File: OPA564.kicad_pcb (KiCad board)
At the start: 2 copper layers, 111 x 61 mm, 29 parts, among them J1 Conn_Coaxial, J4 Conn_Coaxial, J6 Conn_Coaxial, U1 OPA564AIDWPR, U2 OPA564AIDWPR, U3 OPA564AIDWPR

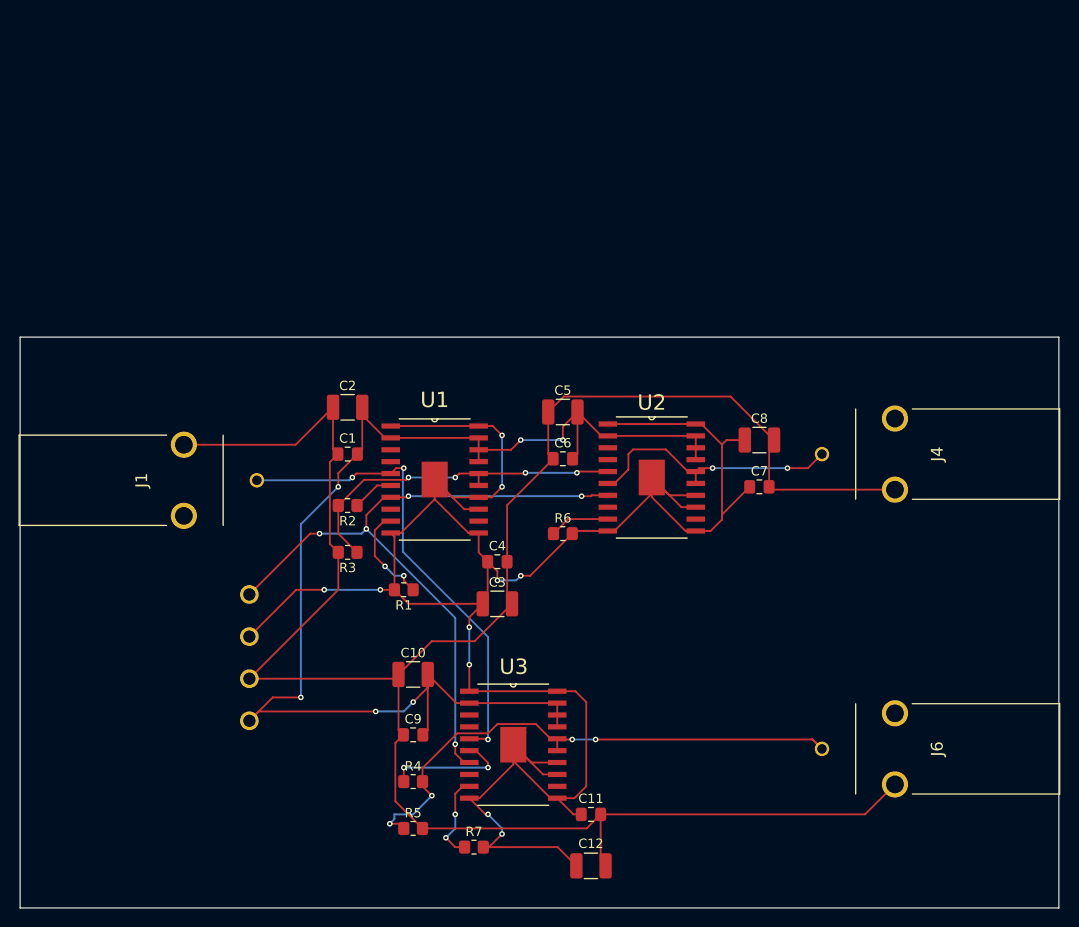
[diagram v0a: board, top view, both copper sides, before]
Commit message: OPA564 without Voltage Follower
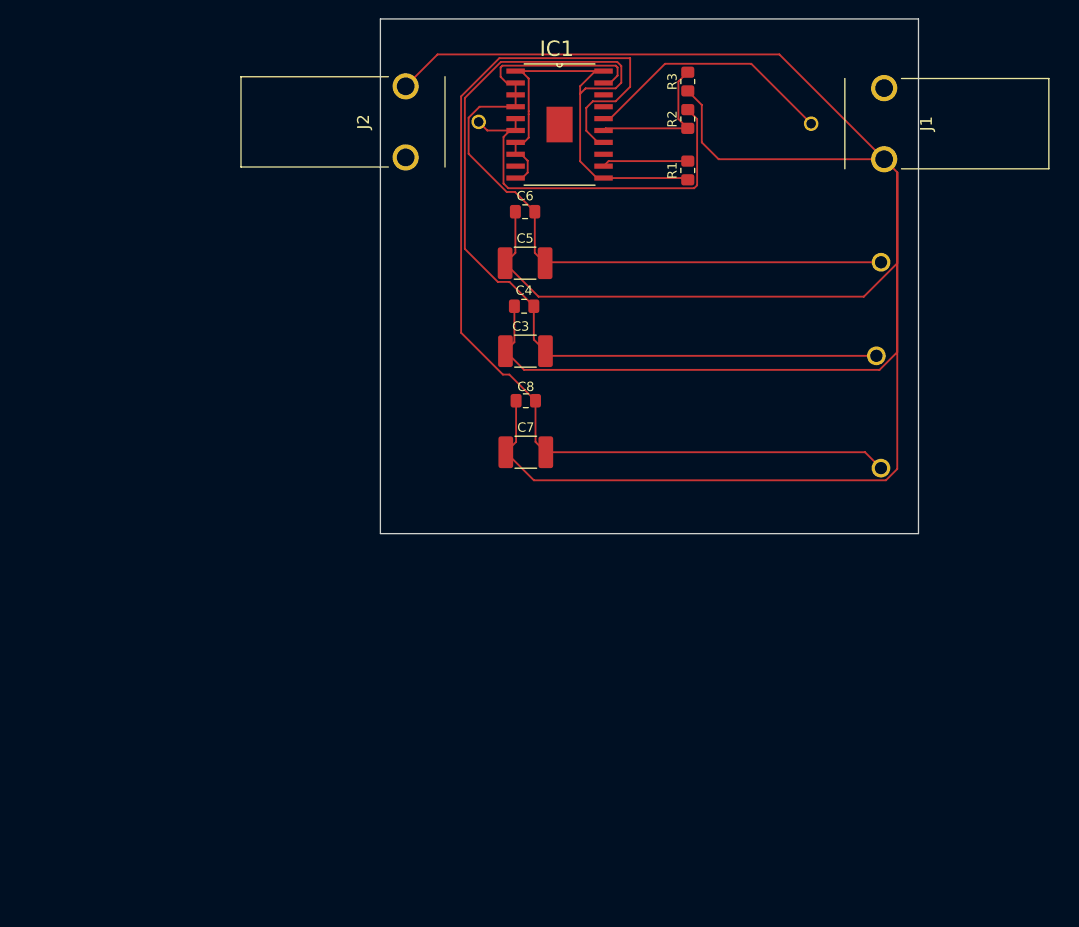
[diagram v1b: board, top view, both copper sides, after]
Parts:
- removed the ? at (118.0, 94.0)
- removed the ? at (118.0, 89.5)
- removed the ? at (118.0, 85.0)
- removed the ? at (118.0, 80.5)
- removed C1, C11, C9: 0.1 uF, Capacitor_SMD:C_0805_2012Metric_Pad1.18x1.45mm_HandSolder
- removed C10, C12, C2: 47 uF, Capacitor_SMD:C_1210_3225Metric_Pad1.33x2.70mm_HandSolder
- removed J4, J6: Conn_Coaxial, 731000154:731000154
- removed R4, R5: 1 kOhms, Resistor_SMD:R_0805_2012Metric_Pad1.20x1.40mm_HandSolder
- removed R6, R7: 14.2 kOhms, Resistor_SMD:R_0805_2012Metric_Pad1.20x1.40mm_HandSolder
- removed U1, U2, U3: OPA564AIDWPR, OPA564AIDWP:SOIC127P1040X265-21N
- added ?: , , F.Cu at (185.5, 45.0)
- added ?: , , F.Cu at (185.5, 67.0)
- added ?: , , F.Cu at (185.0, 55.0)
- added IC1: OPA564AIDWD, OPA564AIDWP:SOIC127P1040X265-21N, F.Cu at (151.1, 30.3)
- added J2: Conn_Coaxial, 731000154:731000154, F.Cu at (142.5, 30.0)
- C3, C5: value 47 uF -> 47 uC; footprint Capacitor_SMD:C_1210_3225Metric_Pad1.33x2.70mm_HandSolder -> Capacitor_SMD:C_1812_4532Metric_Pad1.57x3.40mm_HandSolder
- C4, C6: value 0.1 uF -> 0.1 uC
- C7: value 0.1 uF -> 47 uC; footprint Capacitor_SMD:C_0805_2012Metric_Pad1.18x1.45mm_HandSolder -> Capacitor_SMD:C_1812_4532Metric_Pad1.57x3.40mm_HandSolder
- C8: value 47 uF -> 0.1 uC; footprint Capacitor_SMD:C_1210_3225Metric_Pad1.33x2.70mm_HandSolder -> Capacitor_SMD:C_0805_2012Metric_Pad1.18x1.45mm_HandSolder
- moved J1 70.4 mm to (178.0, 30.2), turned to 90 degrees
- moved R3 62.1 mm to (164.8, 25.7), turned to 90 degrees
- moved R2 55.0 mm to (164.8, 29.7), turned to 90 degrees
- moved R1 54.1 mm to (164.8, 35.2), turned to 90 degrees
- moved C4 27.4 mm to (147.4, 49.7)
- moved C3 27.2 mm to (147.5, 54.5)
- moved C6 26.7 mm to (147.5, 39.6)
- moved C8 25.3 mm to (147.5, 59.8)
- moved C7 25.2 mm to (147.5, 65.3)
- moved C5 16.4 mm to (147.5, 45.1)
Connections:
- net +12V renamed +12 Volts
- C3 pad 1: -12V -> GND
- C3 pad 2: GND -> -12 Volts
- C4 pad 1: -12V -> GND
- C4 pad 2: GND -> -12 Volts
- C7 pad 1: -12V -> GND
- C7 pad 2: GND -> -8 Volts
- C8 pad 1: -12V -> GND
- C8 pad 2: GND -> -8 Volts
- R1 pad 1: Net-(U1-ISET) -> -12 Volts
- R1 pad 2: -12V -> Net-(IC1-ISET)
- R2 pad 1: Net-(U1--IN) -> Net-(IC1--IN)
- R2 pad 2: Net-(U2-+IN) -> Net-(IC1-VOUT_1)
- R3 pad 1: Net-(U2-+IN) -> GND
- R3 pad 2: GND -> Net-(IC1--IN)
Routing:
- net -12V: track 252.4 -> 0.00 mm, vias 10 -> 0
- net -12 Volts: track 0.00 -> 140.9 mm
- net -8 Volts: track 0.00 -> 111.9 mm
- net -8V: track 73.4 -> 0.00 mm, vias 5 -> 0
- net GND: track 227.7 -> 295.2 mm
- net Net-(J6-In): track 59.6 -> 0.00 mm, vias 4 -> 0
- net +12 Volts: track 138.5 -> 80.9 mm, vias 6 -> 0
- net Net-(IC1-VOUT_1): track 0.00 -> 41.7 mm
- net Net-(U2-+IN): track 37.4 -> 0.00 mm, vias 4 -> 0
- net Net-(J4-In): track 28.4 -> 0.00 mm, vias 2 -> 0
- net Signal Input: track 51.1 -> 27.3 mm, vias 3 -> 0
- net Net-(IC1--IN): track 0.00 -> 15.9 mm
- net Net-(U3--IN): track 13.6 -> 0.00 mm, vias 2 -> 0
- net Net-(U1-ISET): track 10.7 -> 0.00 mm, vias 2 -> 0
- net Net-(U3-ISET): track 9.37 -> 0.00 mm, vias 2 -> 0
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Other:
- board size 111 x 61 mm -> 57.5 x 55 mm

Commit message: zone areas
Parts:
- moved ? 33.6 mm to (169.8, 74.7)
- moved ? 33.6 mm to (169.8, 96.7)
- moved ? 33.6 mm to (169.3, 84.7)
- moved C3 33.6 mm to (131.8, 84.2)
- moved C4 33.6 mm to (131.6, 79.4)
- moved C7 33.6 mm to (131.8, 95.0)
- moved C8 33.6 mm to (131.8, 89.5)
- moved J1 33.6 mm to (162.3, 59.9)
- moved J2 33.6 mm to (126.8, 59.7)
- moved R1 33.6 mm to (149.1, 64.9)
- moved R2 33.6 mm to (149.1, 59.4)
- moved R3 33.6 mm to (149.1, 55.4)
- moved C5 33.6 mm to (131.7, 74.8)
- moved C6 33.6 mm to (131.7, 69.3)
- moved IC1 33.6 mm to (135.4, 60.0)
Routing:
- added copper zone on F.Cu, net GND
